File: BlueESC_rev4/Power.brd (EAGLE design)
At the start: 24.4 x 36 mm, 46 parts, among them Q1 BC817-40W, Q2 BC817-40W, Q3 BC817-40W, Q4 SI7370, Q5 SI7370, Q6 SI7370, Q7 SI7370, Q8 SI7370, Q9 SI7370

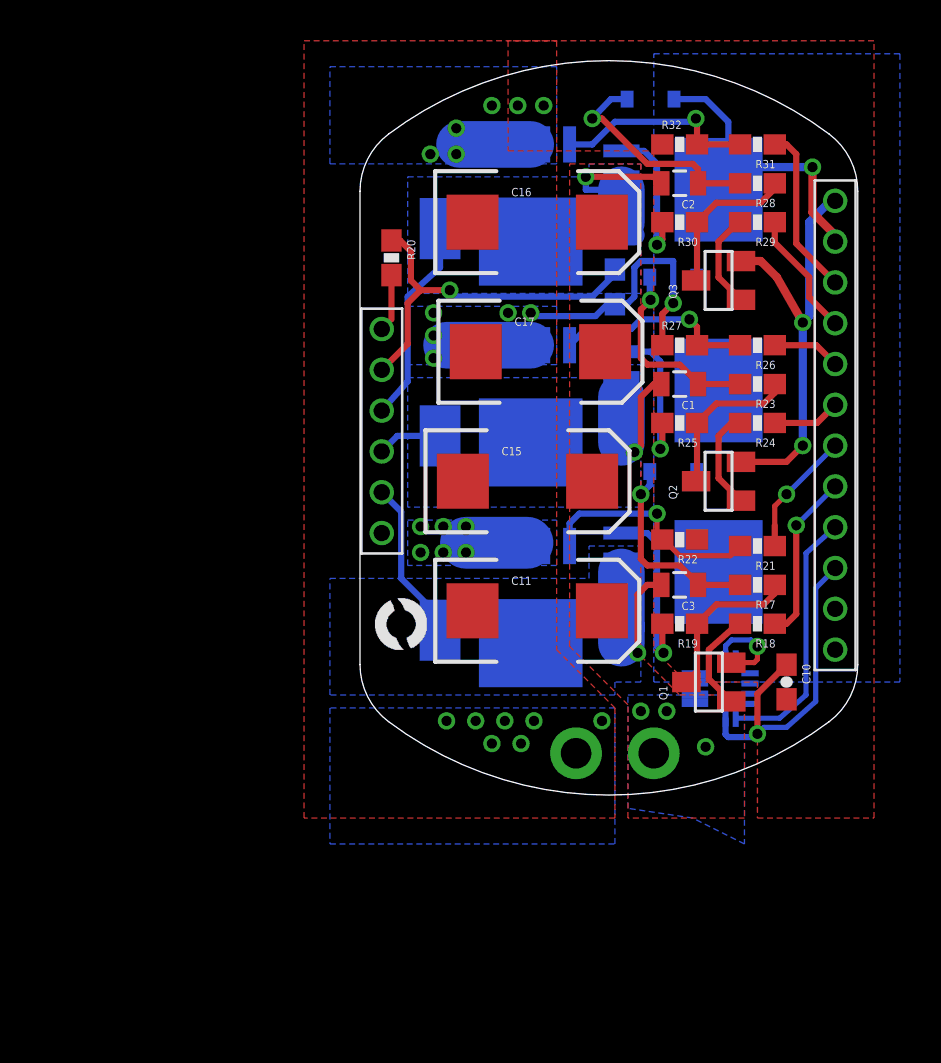
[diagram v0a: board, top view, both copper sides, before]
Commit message: Major updates on revision 4 include rearranged components, removal of programming pins, and new board shapes.
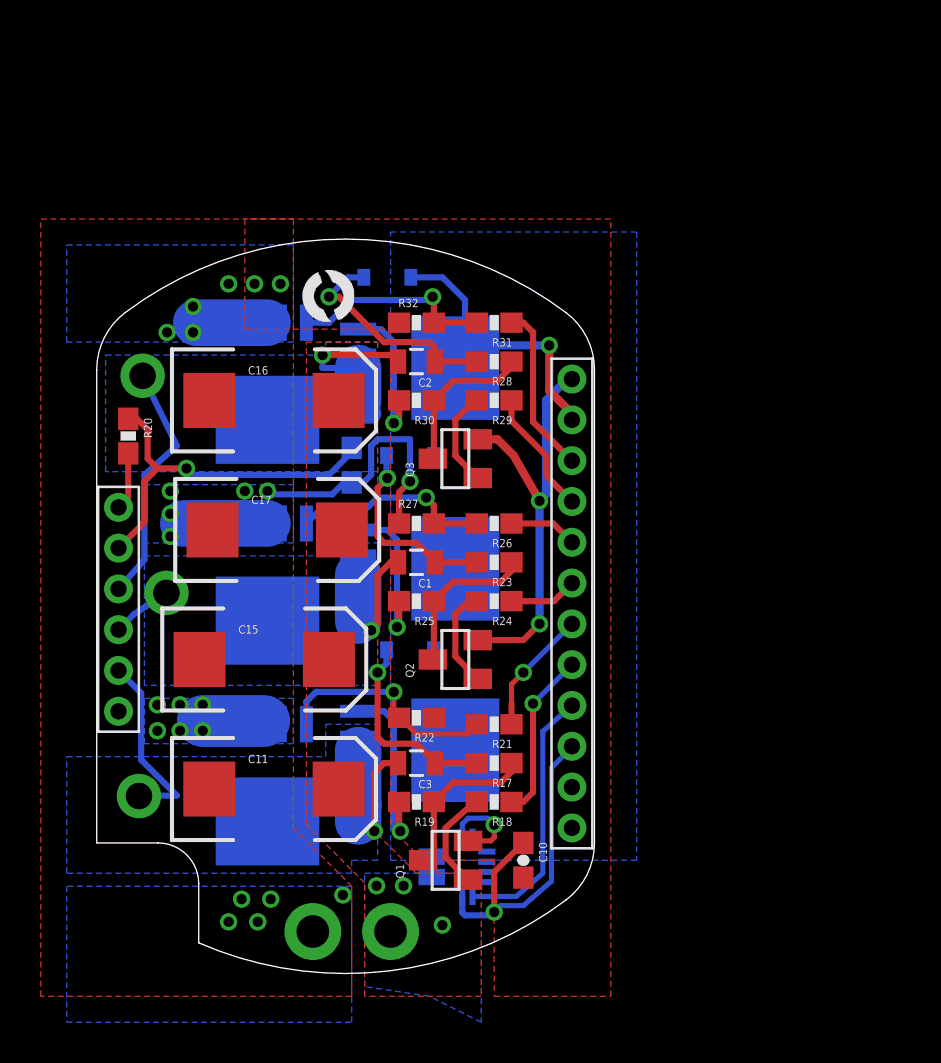
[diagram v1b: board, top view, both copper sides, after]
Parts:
- U$5, U$6, U$7: value PAD2X3MM -> PAD18AWG; device BR-Eagle-Library:PAD-2X3MM -> BR-Eagle-Library:PAD-PTH-18AWG-1
- moved U$5 16.8 mm to (2.07, 8.70)
- moved U$9 16.5 mm to (10.1, 32.0)
- moved U$7 16.3 mm to (2.25, 29.3)
- moved C10 15.6 mm to (20.9, 5.55)
- moved C17 15.6 mm to (8.85, 21.7)
- moved D3 15.6 mm to (14.2, 34.1)
- moved Q1 15.6 mm to (17.1, 5.55)
- moved Q2 15.6 mm to (17.6, 15.4)
- moved Q3 15.6 mm to (17.6, 25.2)
- moved R17 15.6 mm to (19.5, 10.3)
- moved R20 15.6 mm to (1.54, 26.3)
- moved R24 15.6 mm to (19.5, 18.2)
- moved R26 15.6 mm to (19.5, 22.1)
- moved R28 15.6 mm to (19.5, 30.0)
- moved R31 15.6 mm to (19.5, 31.9)
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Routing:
- net PHASE_C: track 20.1 -> 22.1 mm
- net PHASE_A: track 17.3 -> 18.5 mm
- net GND: vias 28 -> 26
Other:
- outline, holes or cut-outs redrawn

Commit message: Minor changes before ordering production boards.
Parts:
- moved U$1 0.50 mm to (14.6, 2.53)
- moved U$2 0.50 mm to (10.4, 2.53)
- moved U$7 0.45 mm to (1.93, 29.6)
- moved U$6 0.16 mm to (3.58, 18.7)
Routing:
- net GND: vias 26 -> 25
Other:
- board text added: "BLUESC-ELEC-POWER-X1C"
- board text removed: "BLUESC-ELEC-POWER-X1B"
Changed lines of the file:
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@@
 <setting verticaltext="up"/>
 </settings>
-<grid distance="0.05" unitdist="inch" unit="inch" style="lines" multiple="1" display="yes" altdistance="0.001" altunitdist="inch" altunit="inch"/>
+<grid distance="0.05" unitdist="inch" unit="inch" style="lines" multiple="1" display="yes" altdistance="0.00625" altunitdist="inch" altunit="inch"/>
 <layers>
 <layer number="1" name="Top" color="4" fill="1" visible="yes" active="yes"/>
@@
 <board>
 <plain>
-<text x="2.49555" y="8.88365" size="1.27" layer="52" rot="MR270">A</text>
-<text x="2.6543" y="18.5674" size="1.27" layer="52" rot="MR270">B</text>
+<text x="5.03555" y="8.24865" size="1.27" layer="52" rot="MR270">A</text>
+<text x="4.08305" y="17.2974" size="1.27" layer="52" rot="MR270">B</text>
 <text x="2.49555" y="28.56865" size="1.27" layer="52" rot="MR270">C</text>
-<text x="20.8407" y="28.8417" size="0.6096" layer="52" rot="MR270">BLUESC-ELEC-POWER-X1B</text>
+<text x="20.8407" y="28.8417" size="0.6096" layer="52" rot="MR270">BLUESC-ELEC-POWER-X1C</text>
 <text x="7.89305" y="0.4699" size="1.6764" layer="51">-</text>
 <text x="17.41805" y="2.21615" size="1.6764" layer="51" rot="R180">+</text>
@@
 <element name="R33" library="SparkFun-Resistors" package="0603-RES" value="10K NTC" x="12.4968" y="24.9174" rot="MR90"/>
 <element name="U$5" library="BR-Eagle-Library" package="PAD-PTH-18AWG-1" value="PAD18AWG" x="2.0701" y="8.6995" rot="MR270"/>
-<element name="U$6" library="BR-Eagle-Library" package="PAD-PTH-18AWG-1" value="PAD18AWG" x="3.4163" y="18.6563" rot="MR90"/>
-<element name="U$7" library="BR-Eagle-Library" package="PAD-PTH-18AWG-1" value="PAD18AWG" x="2.2479" y="29.2989" rot="MR270"/>
+<element name="U$6" library="BR-Eagle-Library" package="PAD-PTH-18AWG-1" value="PAD18AWG" x="3.57505" y="18.6563" rot="MR90"/>
+<element name="U$7" library="BR-Eagle-Library" package="PAD-PTH-18AWG-1" value="PAD18AWG" x="1.9304" y="29.6164" rot="MR270"/>
 <element name="C11" library="SparkFun-Capacitors" package="EIA7343" value="100uF" x="8.6868" y="9.0424"/>
-<element name="U$1" library="BR-Eagle-Library" package="PAD-PTH-MED-1" value="PADPTH-MED" x="14.4018" y="2.0574"/>
-<element name="U$2" library="BR-Eagle-Library" package="PAD-PTH-MED-1" value="PADPTH-MED" x="10.5918" y="2.0574"/>
+<element name="U$1" library="BR-Eagle-Library" package="PAD-PTH-MED-1" value="PADPTH-MED" x="14.56055" y="2.53365"/>
+<element name="U$2" library="BR-Eagle-Library" package="PAD-PTH-MED-1" value="PADPTH-MED" x="10.43305" y="2.53365"/>
 <element name="U$3" library="BR-Eagle-Library" package="12-WFQFN" value="ACS7XX12-WFQFN" x="17.73555" y="5.2324" rot="MR180"/>
 <element name="U$4" library="BR-Eagle-Library" package="HEADER-2MM-6POS" value="HEADER-62MM" x="1.0668" y="12.8524" rot="R90"/>
@@
 <wire x1="4.8768" y1="31.9024" x2="8.3693" y2="31.9024" width="2.286" layer="16"/>
 <polygon width="0.3048" layer="16" isolate="0.254" thermals="no">
-<vertex x="12.4968" y="-2.3876"/>
-<vertex x="12.4968" y="4.2799"/>
+<vertex x="12.33805" y="-2.3876"/>
+<vertex x="12.33805" y="4.2799"/>
 <vertex x="-1.4732" y="4.2799"/>
 <vertex x="-1.4732" y="-2.3876"/>
 </polygon>
-<via x="8.52805" y="3.6449" extent="1-16" drill="0.5"/>
-<via x="7.0993" y="3.6449" extent="1-16" drill="0.5"/>
-<via x="7.89305" y="2.53365" extent="1-16" drill="0.5"/>
-<via x="6.4643" y="2.53365" extent="1-16" drill="0.5"/>
-<via x="12.065" y="3.8481" extent="1-16" drill="0.5"/>
+<via x="7.4168" y="3.6449" extent="1-16" drill="0.5"/>
+<via x="5.98805" y="3.6449" extent="1-16" drill="0.5"/>
+<via x="7.4168" y="2.3749" extent="1-16" drill="0.5"/>
+<via x="5.98805" y="2.3749" extent="1-16" drill="0.5"/>
 <via x="2.9718" y="13.1699" extent="1-16" drill="0.5"/>
 <via x="2.9718" y="11.8999" extent="1-16" drill="0.5"/>
@@
 <via x="4.71805" y="32.69615" extent="1-16" drill="0.5"/>
 <polygon width="0.3048" layer="1" isolate="0.254">
-<vertex x="12.4968" y="-1.1176"/>
+<vertex x="12.33805" y="-1.1176"/>
 <vertex x="-2.7432" y="-1.1176"/>
 <vertex x="-2.7432" y="36.9824"/>
 <vertex x="9.6393" y="36.9824"/>
-<vertex x="9.6393" y="7.1374"/>
-<vertex x="12.4968" y="4.2799"/>
+<vertex x="9.6393" y="6.97865"/>
+<vertex x="12.33805" y="4.43865"/>
 </polygon>
 <wire x1="12.4968" y1="24.0674" x2="12.12305" y2="24.0674" width="0.3048" layer="16"/>
@@
 <polygon width="0.3048" layer="16" isolate="0.254" thermals="no">
 <vertex x="13.7668" y="5.5499"/>
-<vertex x="12.4968" y="5.5499"/>
-<vertex x="12.4968" y="4.9149"/>
+<vertex x="12.33805" y="5.5499"/>
+<vertex x="12.33805" y="4.9149"/>
 <vertex x="-1.4732" y="4.9149"/>
 <vertex x="-1.4732" y="10.6299"/>
@@
 <via x="13.4493" y="16.82115" extent="1-16" drill="0.5"/>
 <wire x1="13.4493" y1="16.82115" x2="12.8143" y2="17.2974" width="0.3048" layer="16"/>
-<wire x1="3.4163" y1="18.6563" x2="1.8293" y2="17.6149" width="0.3048" layer="16"/>
+<wire x1="3.57505" y1="18.6563" x2="1.8293" y2="17.6149" width="0.3048" layer="16"/>
 <wire x1="1.8293" y1="17.6149" x2="1.0668" y2="16.8524" width="0.3048" layer="16"/>
 </signal>
@@
 <wire x1="11.06805" y1="30.3149" x2="11.06805" y2="29.6799" width="0.3048" layer="16"/>
 <wire x1="11.06805" y1="29.6799" x2="12.8143" y2="29.6799" width="0.3048" layer="16"/>
-<wire x1="2.2479" y1="29.2989" x2="3.9243" y2="25.8699" width="0.3048" layer="16"/>
+<wire x1="1.9304" y1="29.6164" x2="3.9243" y2="25.8699" width="0.3048" layer="16"/>
 <wire x1="3.9243" y1="25.8699" x2="2.3368" y2="24.44115" width="0.3048" layer="16"/>
 <wire x1="2.3368" y1="24.44115" x2="2.3368" y2="20.28115" width="0.3048" layer="16"/>
@@
 <contactref element="U$3" pad="IP+2"/>
 <polygon width="0.3048" layer="16" isolate="0.254" thermals="no">
-<vertex x="13.1318" y="-0.64135"/>
-<vertex x="13.1318" y="4.9149"/>
+<vertex x="12.97305" y="-0.64135"/>
+<vertex x="12.97305" y="4.9149"/>
 <vertex x="18.8468" y="4.9149"/>
 <vertex x="18.8468" y="-2.3876"/>
@@
 <contactref element="C17" pad="A"/>
 <polygon width="0.3048" layer="1" isolate="0.254">
-<vertex x="13.1318" y="-1.1176"/>
-<vertex x="13.1318" y="4.43865"/>
+<vertex x="12.97305" y="-1.1176"/>
+<vertex x="12.97305" y="4.5974"/>
 <vertex x="10.2743" y="7.29615"/>
 <vertex x="10.2743" y="30.9499"/>
@@
 <vertex x="18.8468" y="-1.1176"/>
 </polygon>
-<via x="13.716" y="4.29895" extent="1-16" drill="0.5"/>
-<via x="15.0368" y="4.29895" extent="1-16" drill="0.5"/>
-<via x="16.9418" y="2.3749" extent="1-16" drill="0.5"/>
+<via x="17.73555" y="1.9177" extent="1-16" drill="0.5"/>
+<via x="16.9418" y="3.16865" extent="1-16" drill="0.5"/>
 </signal>
 <signal name="VCC5V-1">
